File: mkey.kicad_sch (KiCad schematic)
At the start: 161 parts, among them J1 USB_C_REP_2.0, SW1 SW_Push, SW2 SW_Push, U1 ESP32-S3-WROOM-1, U5 SY8088

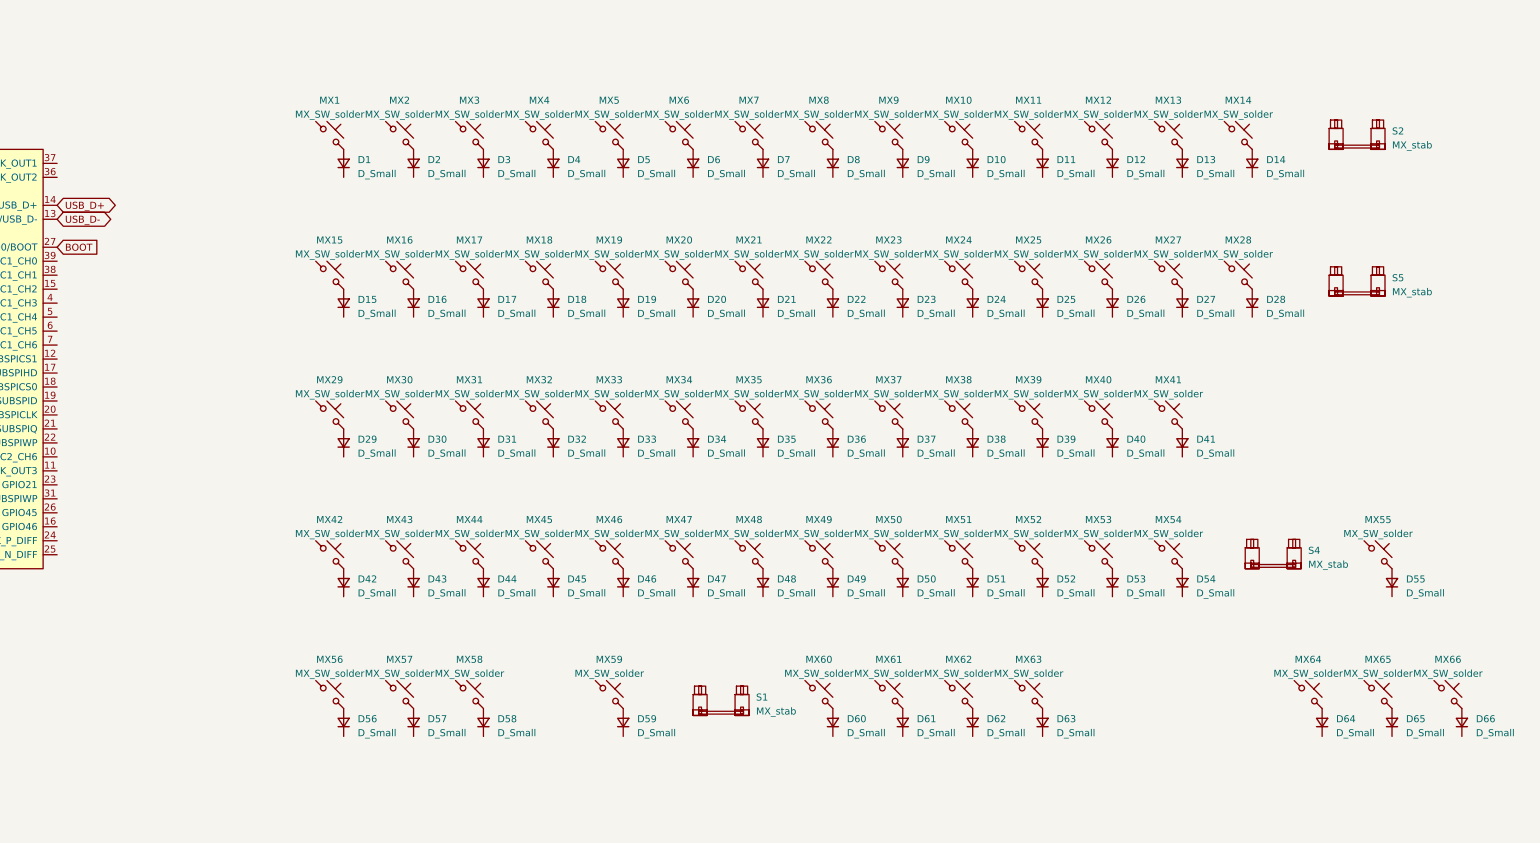
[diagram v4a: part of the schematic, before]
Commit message: wire matrix, route some columns and rows, need to rewire some columns on the bottom row of keys to make routing easier
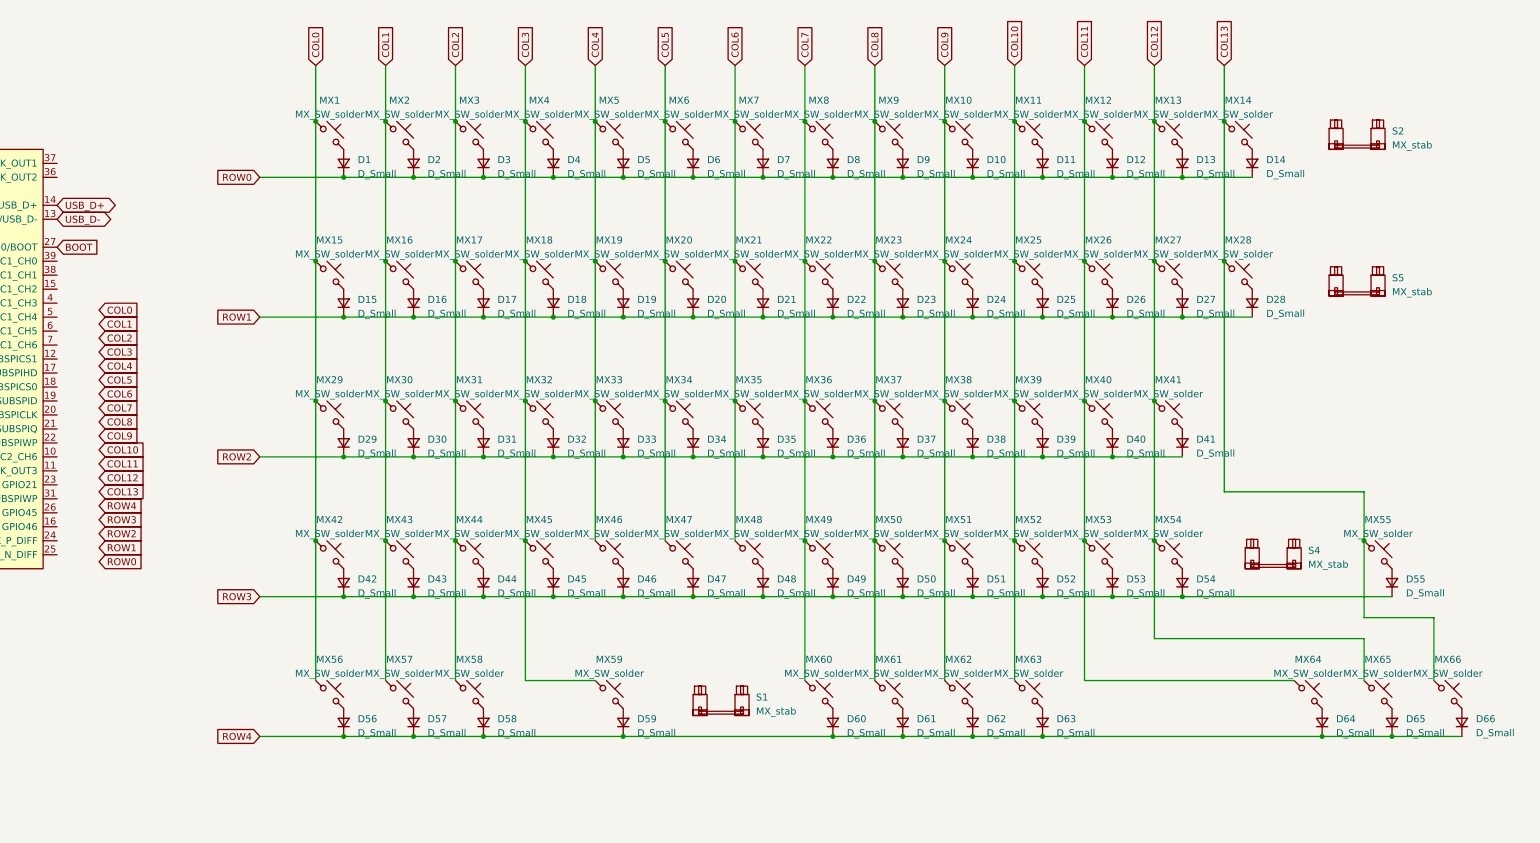
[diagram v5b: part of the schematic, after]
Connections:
- net ROW1: now reaches D23.1 (K)
- net ROW1: now also D15.1 (K), D16.1 (K), D17.1 (K), D18.1 (K), D19.1 (K), D20.1 (K), D21.1 (K), D22.1 (K), D24.1 (K), D25.1 (K), D26.1 (K), D27.1 (K), D28.1 (K)
- net ROW0: now reaches D3.1 (K)
- net ROW0: now also D1.1 (K), D10.1 (K), D11.1 (K), D12.1 (K), D13.1 (K), D14.1 (K), D2.1 (K), D4.1 (K), D5.1 (K), D6.1 (K), D7.1 (K), D8.1 (K), D9.1 (K)
- net COL12: now reaches MX27.1
- net COL12: now also MX13.1, MX41.1, MX54.1, MX65.1
- net ROW3: now reaches D46.1 (K)
- net ROW3: now also D42.1 (K), D43.1 (K), D44.1 (K), D45.1 (K), D47.1 (K), D48.1 (K), D49.1 (K), D50.1 (K), D51.1 (K), D52.1 (K), D53.1 (K), D54.1 (K), D55.1 (K)
- net COL3: now reaches MX59.1
- net COL3: now also MX18.1, MX32.1, MX4.1, MX45.1
- net COL5: now reaches MX47.1
- net COL5: now also MX20.1, MX34.1, MX6.1
- net COL13: now reaches MX66.1
- net COL13: now also MX14.1, MX28.1, MX55.1
- net COL1: now reaches MX16.1
- net COL1: now also MX2.1, MX30.1, MX43.1, MX57.1
- net ROW2: now reaches D31.1 (K)
- net ROW2: now also D29.1 (K), D30.1 (K), D32.1 (K), D33.1 (K), D34.1 (K), D35.1 (K), D36.1 (K), D37.1 (K), D38.1 (K), D39.1 (K), D40.1 (K), D41.1 (K)
- net COL9: now reaches MX10.1
- net COL9: now also MX24.1, MX38.1, MX51.1, MX62.1
- net ROW4: now reaches D65.1 (K)
- net ROW4: now also D56.1 (K), D57.1 (K), D58.1 (K), D59.1 (K), D60.1 (K), D61.1 (K), D62.1 (K), D63.1 (K), D64.1 (K), D66.1 (K)
- net COL0: now reaches MX15.1
- net COL0: now also MX1.1, MX29.1, MX42.1, MX56.1
- net COL7: now reaches MX49.1
- net COL7: now also MX22.1, MX36.1, MX60.1, MX8.1
- net COL2: now reaches MX58.1
- net COL2: now also MX17.1, MX3.1, MX31.1, MX44.1
- net COL4: now reaches MX5.1
- net COL4: now also MX19.1, MX33.1, MX46.1
- net COL11: now reaches MX53.1
- net COL11: now also MX12.1, MX26.1, MX40.1, MX64.1
- net COL8: now reaches MX50.1
- net COL8: now also MX23.1, MX37.1, MX61.1, MX9.1
- net COL6: now reaches MX21.1
- net COL6: now also MX35.1, MX48.1, MX7.1
- net COL10: now reaches MX39.1
- net COL10: now also MX11.1, MX25.1, MX52.1, MX63.1

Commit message: finish routing matrix, rework mcu routing and start TODO
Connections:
- net COL3: no longer MX59.1
- net COL5: now also MX59.1
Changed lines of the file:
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@@
   (junction (at 302.26 111.76) (diameter 0) (color 0 0 0 0)
   )
+  (junction (at 251.46 137.16) (diameter 0) (color 0 0 0 0)
+  )
   (junction (at 340.36 137.16) (diameter 0) (color 0 0 0 0)
   )
@@
   )
   (junction (at 370.84 172.72) (diameter 0) (color 0 0 0 0)
-  )
-  (junction (at 226.06 137.16) (diameter 0) (color 0 0 0 0)
   )
   (no_connect (at 97.79 250.19))
@@
     (stroke (width 0) (type default))
   )
-  (wire (pts (xy 226.06 162.56) (xy 238.76 162.56))
-    (stroke (width 0) (type default))
-  )
   (polyline (pts (xy 69.85 210.82) (xy 153.67 210.82))
     (stroke (width 0) (type default))
@@
     (stroke (width 0) (type default))
   )
+  (wire (pts (xy 251.46 152.4) (xy 238.76 152.4))
+    (stroke (width 0) (type default))
+  )
   (wire (pts (xy 213.36 137.16) (xy 213.36 162.56))
     (stroke (width 0) (type default))
@@
     (stroke (width 0) (type default))
   )
+  (wire (pts (xy 238.76 152.4) (xy 238.76 162.56))
+    (stroke (width 0) (type default))
+  )
   (wire (pts (xy 264.16 86.36) (xy 264.16 111.76))
     (stroke (width 0) (type default))
@@
     (stroke (width 0) (type default))
   )
-  (wire (pts (xy 226.06 137.16) (xy 226.06 162.56))
-    (stroke (width 0) (type default))
-  )
   (wire (pts (xy 181.61 219.71) (xy 189.23 219.71))
     (stroke (width 0) (type default))
@@
     (stroke (width 0) (type default))
   )
+  (wire (pts (xy 251.46 137.16) (xy 251.46 152.4))
+    (stroke (width 0) (type default))
+  )

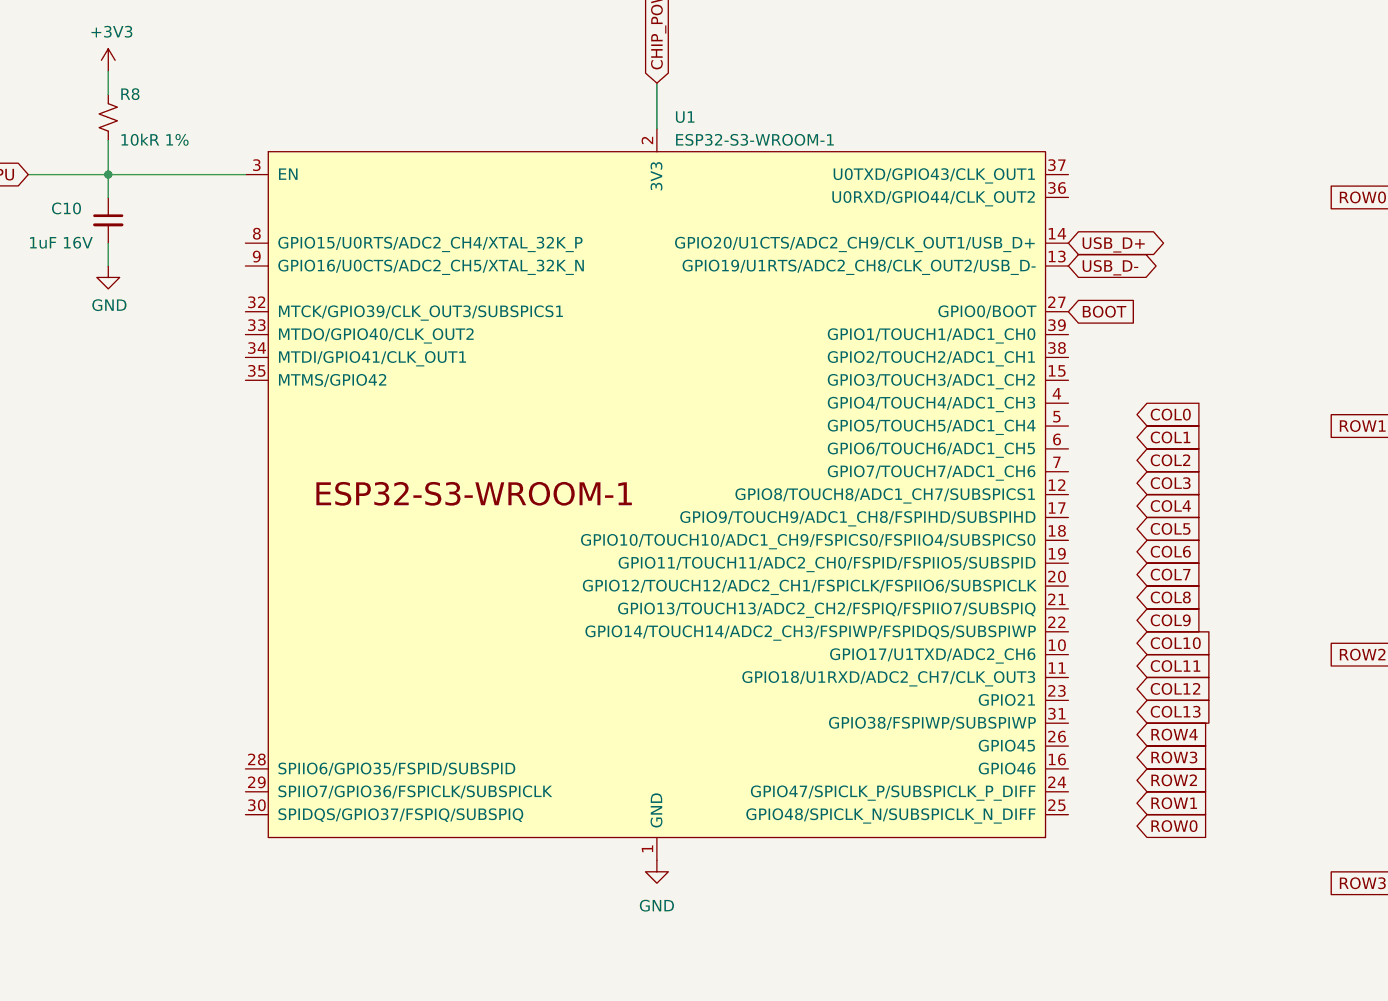
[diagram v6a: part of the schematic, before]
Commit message: initial schematic updates for routing matrix
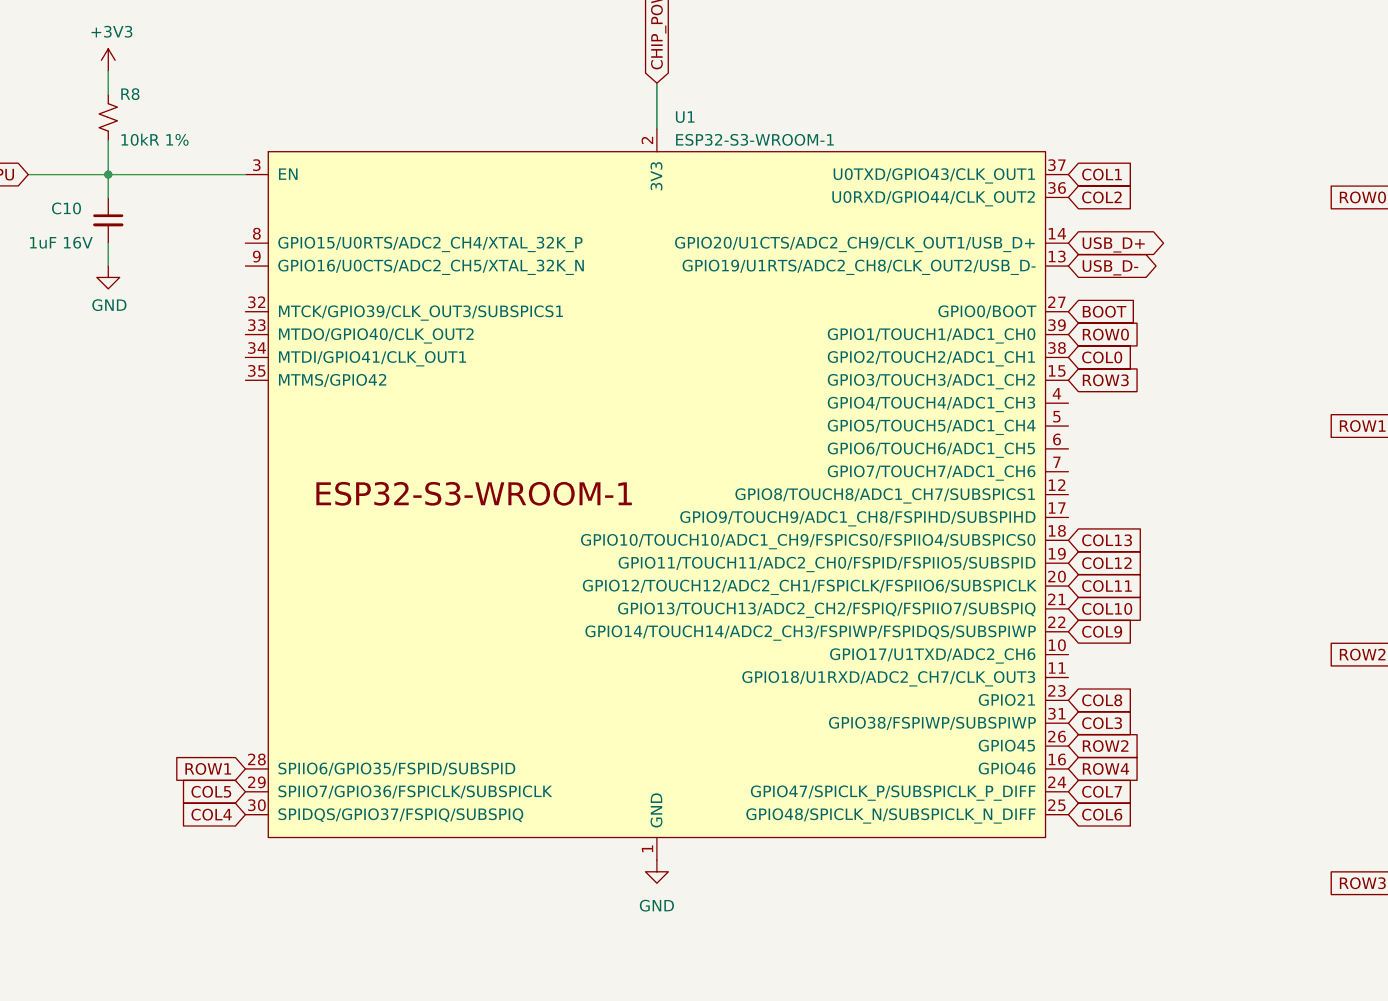
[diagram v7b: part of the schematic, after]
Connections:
- net COL0: now also U1.38 (GPIO2/TOUCH2/ADC1_CH1)
- net COL1: now also U1.37 (U0TXD/GPIO43/CLK_OUT1)
- net COL10: now also U1.21 (GPIO13/TOUCH13/ADC2_CH2/FSPIQ/FSPIIO7/SUBSPIQ)
- net COL11: now also U1.20 (GPIO12/TOUCH12/ADC2_CH1/FSPICLK/FSPIIO6/SUBSPICLK)
- net COL12: now also U1.19 (GPIO11/TOUCH11/ADC2_CH0/FSPID/FSPIIO5/SUBSPID)
- net COL13: now also U1.18 (GPIO10/TOUCH10/ADC1_CH9/FSPICS0/FSPIIO4/SUBSPICS0)
- net COL2: now also U1.36 (U0RXD/GPIO44/CLK_OUT2)
- net COL3: now also U1.31 (GPIO38/FSPIWP/SUBSPIWP)
- net COL4: now also U1.30 (SPIDQS/GPIO37/FSPIQ/SUBSPIQ)
- net COL5: now also U1.29 (SPIIO7/GPIO36/FSPICLK/SUBSPICLK)
- net COL6: now also U1.25 (GPIO48/SPICLK_N/SUBSPICLK_N_DIFF)
- net COL7: now also U1.24 (GPIO47/SPICLK_P/SUBSPICLK_P_DIFF)
- net COL8: now also U1.23 (GPIO21)
- net COL9: now also U1.22 (GPIO14/TOUCH14/ADC2_CH3/FSPIWP/FSPIDQS/SUBSPIWP)
- net ROW0: now also U1.39 (GPIO1/TOUCH1/ADC1_CH0)
- net ROW1: now also U1.28 (SPIIO6/GPIO35/FSPID/SUBSPID)
- net ROW2: now also U1.26 (GPIO45)
- net ROW3: now also U1.15 (GPIO3/TOUCH3/ADC1_CH2)
- net ROW4: now also U1.16 (GPIO46)

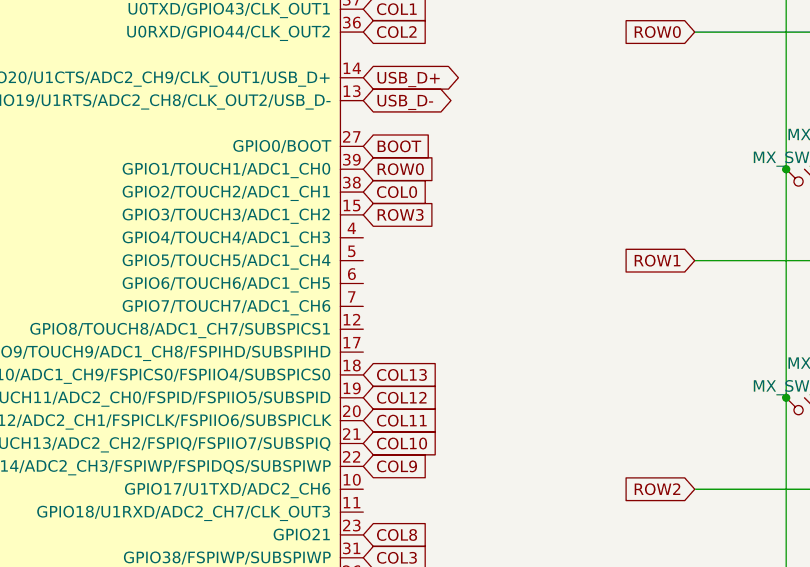
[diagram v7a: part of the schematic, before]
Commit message: routed entire keyboard matrix
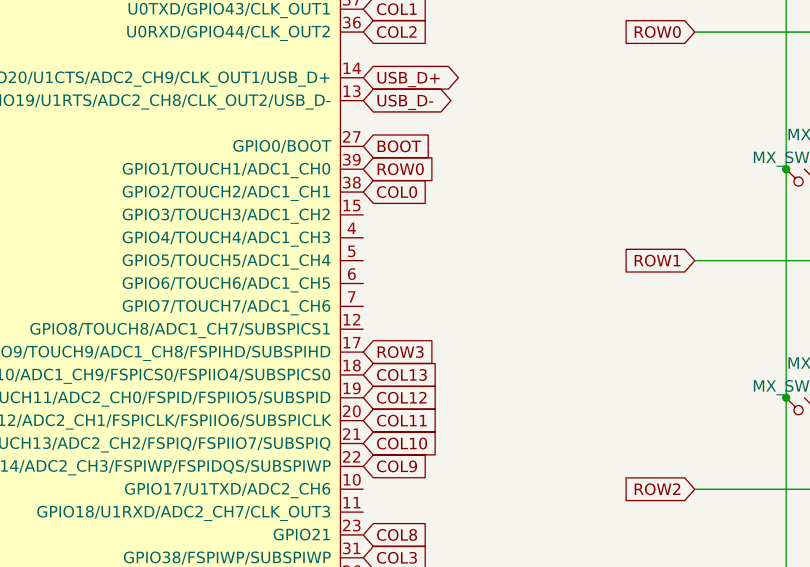
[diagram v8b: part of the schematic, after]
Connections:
- net ROW3: now also U1.17 (GPIO9/TOUCH9/ADC1_CH8/FSPIHD/SUBSPIHD); no longer U1.15 (GPIO3/TOUCH3/ADC1_CH2)
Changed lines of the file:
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@@
     )
   )
-  (global_label "ROW3" (shape input) (at 140.97 91.44 0) (fields_autoplaced)
+  (global_label "ROW3" (shape input) (at 140.97 106.68 0) (fields_autoplaced)
     (effects (font (size 1.27 1.27)) (justify left))
-    (property "Intersheetrefs" "${INTERSHEET_REFS}" (at 149.1372 91.44 0)
+    (property "Intersheetrefs" "${INTERSHEET_REFS}" (at 149.1372 106.68 0)
       (effects (font (size 1.27 1.27)) (justify left) hide)
     )
